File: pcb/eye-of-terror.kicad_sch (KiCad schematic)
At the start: 140 parts, among them J1 Conn_01x02_Socket, J2 G-Switch GT-USB-7055E, J3 Conn_01x04, J4 Conn_01x04, J5 Conn_01x03, J6 Conn_01x02_Socket, Q1 IPT020N10N3, Q2 IPT020N10N3, Q3 IPT020N10N3, Q4 IPT020N10N3, Q5 IPT020N10N3, Q6 IPT020N10N3, SW1 SW_Push, SW2 SW_Push, U1 RP2350B, U2 TD1660, U3 AP63205WU-7, U4 LSM6DS3, U5 W25Q32JVSS, U7 DRV8353HRTAR, Y1 ABM8-272-T3

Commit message: all footprints checked and added
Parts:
- C1, C39: footprint (none) -> Capacitor_SMD:CP_Elec_5x5.4
- J2: footprint (none) -> ul_GT-USB-7055A:CONN_GT-USB-7055A_GSW
- J3, J4: footprint (none) -> Connector_PinHeader_2.54mm:PinHeader_1x04_P2.54mm_Vertical
- J5: footprint (none) -> Connector_PinHeader_2.54mm:PinHeader_1x03_P2.54mm_Vertical
- JP1, JP10, JP11, JP12, JP13, JP14, JP15, JP2, JP3, JP4, JP5, JP6, JP7, JP8, JP9: footprint (none) -> Jumper:SolderJumper-2_P1.3mm_Bridged_RoundedPad1.0x1.5mm
- L1: footprint (none) -> inductor-muRataLQH5BPZ4R7NT0L:IND_LQH5BPZ4R7NT0L
- L2: footprint (none) -> Inductor_SMD:L_Sunlord_MWSA0402S
- SW1, SW2: footprint (none) -> Button_Switch_SMD:SW_Push_SPST_NO_Alps_SKRK
- U2: footprint (none) -> Techcode-Semicon-TD1660:TD1660-SOIC-8
- U3: footprint SOIC_05WU-7_DIO -> AP6320X-WU:SOIC_05WU-7_DIO
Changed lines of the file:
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@@
 			)
 		)
-		(property "Footprint" ""
+		(property "Footprint" "Jumper:SolderJumper-2_P1.3mm_Bridged_RoundedPad1.0x1.5mm"
 			(at 34.29 226.06 0)
 			(effects
@@
 			)
 		)
-		(property "Footprint" ""
+		(property "Footprint" "Connector_PinHeader_2.54mm:PinHeader_1x04_P2.54mm_Vertical"
 			(at 124.46 219.71 0)
 			(effects
@@
 			)
 		)
-		(property "Footprint" ""
+		(property "Footprint" "Jumper:SolderJumper-2_P1.3mm_Bridged_RoundedPad1.0x1.5mm"
 			(at 34.29 236.22 0)
 			(effects
@@
 			)
 		)
-		(property "Footprint" ""
+		(property "Footprint" "Jumper:SolderJumper-2_P1.3mm_Bridged_RoundedPad1.0x1.5mm"
 			(at 309.88 351.79 0)
 			(effects
@@
 			)
 		)
-		(property "Footprint" ""
+		(property "Footprint" "Jumper:SolderJumper-2_P1.3mm_Bridged_RoundedPad1.0x1.5mm"
 			(at 370.84 382.27 0)
 			(effects
@@
 			)
 		)
-		(property "Footprint" ""
+		(property "Footprint" "ul_GT-USB-7055A:CONN_GT-USB-7055A_GSW"
 			(at 107.95 386.08 0)
 			(effects
@@
 			)
 		)
-		(property "Footprint" ""
+		(property "Footprint" "Button_Switch_SMD:SW_Push_SPST_NO_Alps_SKRK"
 			(at 198.12 177.8 0)
 			(effects
@@
 			)
 		)
-		(property "Footprint" ""
+		(property "Footprint" "inductor-muRataLQH5BPZ4R7NT0L:IND_LQH5BPZ4R7NT0L"
 			(at 83.82 289.56 0)
 			(effects
@@
 			)
 		)
-		(property "Footprint" ""
+		(property "Footprint" "Button_Switch_SMD:SW_Push_SPST_NO_Alps_SKRK"
 			(at 212.09 156.21 0)
 			(effects
@@
 			)
 		)
-		(property "Footprint" ""
+		(property "Footprint" "Jumper:SolderJumper-2_P1.3mm_Bridged_RoundedPad1.0x1.5mm"
 			(at 34.29 241.3 0)
 			(effects
@@
 			)
 		)
-		(property "Footprint" ""
+		(property "Footprint" "Jumper:SolderJumper-2_P1.3mm_Bridged_RoundedPad1.0x1.5mm"
 			(at 34.29 238.76 0)
 			(effects
@@
 			)
 		)
-		(property "Footprint" ""
+		(property "Footprint" "Inductor_SMD:L_Sunlord_MWSA0402S"
 			(at 76.2 325.12 0)
 			(effects
@@
 			)
 		)
-		(property "Footprint" ""
+		(property "Footprint" "Connector_PinHeader_2.54mm:PinHeader_1x03_P2.54mm_Vertical"
 			(at 147.32 322.58 0)
 			(effects
@@
 			)
 		)
-		(property "Footprint" ""
+		(property "Footprint" "Jumper:SolderJumper-2_P1.3mm_Bridged_RoundedPad1.0x1.5mm"
 			(at 369.57 351.79 0)
 			(effects
@@
 			)
 		)
-		(property "Footprint" ""
+		(property "Footprint" "Jumper:SolderJumper-2_P1.3mm_Bridged_RoundedPad1.0x1.5mm"
 			(at 157.48 229.87 0)
 			(effects
@@
 			)
 		)
-		(property "Footprint" ""
+		(property "Footprint" "Jumper:SolderJumper-2_P1.3mm_Bridged_RoundedPad1.0x1.5mm"
 			(at 255.27 382.27 0)
 			(effects
@@
 			)
 		)
-		(property "Footprint" ""
+		(property "Footprint" "Jumper:SolderJumper-2_P1.3mm_Bridged_RoundedPad1.0x1.5mm"
 			(at 109.22 245.11 0)
 			(effects
@@
 			)
 		)
-		(property "Footprint" ""
+		(property "Footprint" "Capacitor_SMD:CP_Elec_5x5.4"
 			(at 256.54 208.28 0)
 			(effects
@@
 			)
 		)
-		(property "Footprint" ""
+		(property "Footprint" "Jumper:SolderJumper-2_P1.3mm_Bridged_RoundedPad1.0x1.5mm"
 			(at 311.15 382.27 0)
 			(effects
@@
 			)
 		)
-		(property "Footprint" ""
+		(property "Footprint" "Techcode-Semicon-TD1660:TD1660-SOIC-8"
 			(at 44.45 322.58 0)
 			(effects
@@
 			)
 		)
-		(property "Footprint" ""
+		(property "Footprint" "Jumper:SolderJumper-2_P1.3mm_Bridged_RoundedPad1.0x1.5mm"
 			(at 254 351.79 0)
 			(effects
@@
 			)
 		)
-		(property "Footprint" ""
+		(property "Footprint" "Connector_PinHeader_2.54mm:PinHeader_1x04_P2.54mm_Vertical"
 			(at 124.46 242.57 0)
 			(effects
@@
 			)
 		)
-		(property "Footprint" ""
+		(property "Footprint" "Jumper:SolderJumper-2_P1.3mm_Bridged_RoundedPad1.0x1.5mm"
 			(at 109.22 247.65 0)
 			(effects
@@
 			)
 		)
-		(property "Footprint" ""
+		(property "Footprint" "Capacitor_SMD:CP_Elec_5x5.4"
 			(at 22.86 293.37 0)
 			(effects
@@
 			)
 		)
-		(property "Footprint" ""
+		(property "Footprint" "Jumper:SolderJumper-2_P1.3mm_Bridged_RoundedPad1.0x1.5mm"
 			(at 109.22 224.79 0)
 			(effects
@@
 			)
 		)
-		(property "Footprint" ""
+		(property "Footprint" "Jumper:SolderJumper-2_P1.3mm_Bridged_RoundedPad1.0x1.5mm"
 			(at 109.22 222.25 0)
 			(effects
@@
 			)
 		)
-		(property "Footprint" "SOIC_05WU-7_DIO"
+		(property "Footprint" "AP6320X-WU:SOIC_05WU-7_DIO"
 			(at 44.45 287.02 0)
 			(effects

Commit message: added extra breakout GPIO pins, imported PCB DXF
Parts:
- added J10, J11, J12, J13, J14, J15, J16, J8, J9: Conn_01x03, Connector_PinHeader_2.54mm:PinHeader_1x03_P2.54mm_Vertical, symbol Connector_Generic:Conn_01x03
- added J7: Conn_01x02_Socket, Connector_AMASS:AMASS_XT60-M_1x02_P7.20mm_Vertical, symbol Connector:Conn_01x02_Socket
- added JP16: SolderJumper_2_Bridged, Jumper:SolderJumper-2_P1.3mm_Bridged_RoundedPad1.0x1.5mm, symbol Jumper:SolderJumper_2_Bridged
- added JP17, JP18, JP19, JP20, JP21, JP22, JP23, JP24, JP25: SolderJumper_3_Open, Jumper:SolderJumper-3_P1.3mm_Open_RoundedPad1.0x1.5mm, symbol Jumper:SolderJumper_3_Open
- J3, J4: footprint Connector_PinHeader_2.54mm:PinHeader_1x04_P2.54mm_Vertical -> Connector_PinHeader_1.00mm:PinHeader_1x04_P1.00mm_Vertical
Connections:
- net +3V3: now also JP17.3 (B), JP18.3 (B), JP19.3 (B), JP20.3 (B), JP21.3 (B), JP22.3 (B), JP23.3 (B), JP24.3 (B), JP25.3 (B)
- net +5V: now also JP17.1 (A), JP18.1 (A), JP19.1 (A), JP20.1 (A), JP21.1 (A), JP22.1 (A), JP23.1 (A), JP24.1 (A), JP25.1 (A)
- net +BATT: now also JP16.2 (B); no longer D18.2 (A)
- net +BATT_RAW: now also J7.1 (Pin_1)
- net AGND: now also J10.3 (Pin_3), J11.3 (Pin_3), J12.3 (Pin_3), J13.3 (Pin_3), J14.3 (Pin_3), J15.3 (Pin_3), J16.3 (Pin_3), J7.2 (Pin_2), J8.3 (Pin_3), J9.3 (Pin_3)
- net GPIO24: now reaches U1.25 (GPIO24)
- net GPIO24: now also J11.1 (Pin_1)
- net GPIO34: now reaches U1.43 (GPIO34)
- net GPIO34: now also J12.1 (Pin_1)
- net GPIO35: now reaches U1.44 (GPIO35)
- net GPIO35: now also J13.1 (Pin_1)
- net GPIO37: now reaches U1.46 (GPIO37)
- net GPIO37: now also J14.1 (Pin_1)
- net GPIO38: now reaches U1.47 (GPIO38)
- net GPIO38: now also J15.1 (Pin_1)
- net GPIO39: now reaches U1.48 (GPIO39)
- net GPIO39: now also J16.1 (Pin_1)
- net GPIO1: now reaches U1.78 (GPIO1)
- net GPIO1: now also J8.1 (Pin_1)
- net GPIO2: now reaches U1.79 (GPIO2)
- net GPIO2: now also J9.1 (Pin_1)
- net GPIO3: now reaches U1.80 (GPIO3)
- net GPIO3: now also J10.1 (Pin_1)
- new net: J8.2 (Pin_2), JP17.2 (C)
- new net: D18.2 (A), JP16.1 (A)
- new net: J10.2 (Pin_2), JP19.2 (C)
- new net: J16.2 (Pin_2), JP25.2 (C)
- new net: J11.2 (Pin_2), JP20.2 (C)
- new net: J15.2 (Pin_2), JP24.2 (C)
- new net: J9.2 (Pin_2), JP18.2 (C)
- new net: J14.2 (Pin_2), JP23.2 (C)
- new net: J13.2 (Pin_2), JP22.2 (C)
- new net: J12.2 (Pin_2), JP21.2 (C)
- no-connect marks 13 -> 4
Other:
- note added: "Battery Plugs"
- note added: "Cut this jumper if the LED always being on gets too annoying."
- note added: "Extra GPIO Breakout Pins"
- note added: "This pinout follows Adafruit's STEMMA QT cables. The connectors they use are JST-SH 4-pin, 1mm pitch."
- note removed: "Battery Plug"
- note removed: "This pinout follows Adafruit's STEMMA QT cables."
- moved on the sheet: D18, J1, R40

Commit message: WIP layout, most components placed
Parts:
- added H1, H10, H11, H12, H13, H14, H15, H16, H17, H18, H19, H2, H20, H21, H22, H23, H24, H25, H26, H27, H28, H29, H3, H30, H31, H32, H33, H34, H35, H36, H37, H38, H39, H4, H40, H41, H42, H43, H44, H45, H46, H47, H48, H49, H5, H50, H51, H52, H53, H54, H6, H7, H8, H9: MountingHole, MountingHole:MountingHole_3.2mm_M3, symbol Mechanical:MountingHole
- added NT1: NetTie_3, NetTie:NetTie-3_SMD_Pad2.0mm, symbol Device:NetTie_3
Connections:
- net +BATT_RAW: now also J1.2 (Pin_2), J7.2 (Pin_2); no longer J1.1 (Pin_1), J7.1 (Pin_1)
- net AGND: now also NT1.2; no longer C1.2, C10.1, C11.1, C12.1, C13.1, C14.1, C15.1, C16.1, C17.1, C18.1, C19.1, C20.1, C21.1, C22.1, C23.1, C24.1, C25.1, C26.1, C27.1, C28.1, C29.1, C3.2, C30.1, C33.1, C34.1, C36.1, C37.1, C38.1, C39.1, C4.2, C6.2, C7.2, C8.2, D1.2 (A2), D2.2 (A), J1.2 (Pin_2), J10.3 (Pin_3), J11.3 (Pin_3), J12.3 (Pin_3), J13.3 (Pin_3), J14.3 (Pin_3), J15.3 (Pin_3), J16.3 (Pin_3), J2.A1/B12 (GND), J2.B1/A12 (GND), J3.1 (Pin_1), J4.1 (Pin_1), J5.2 (Pin_2), J7.2 (Pin_2), J8.3 (Pin_3), J9.3 (Pin_3), R1.1, R10.2, R17.2, R18.2, R19.2, R2.1, R21.2, R23.2, R24.2, R25.2, R26.2, R27.2, R28.2, R29.2, R30.2, R31.2, R32.2, R33.2, R34.2, R35.2, R36.2, R37.2, R38.2, R39.2, R4.2, R40.1, R5.2, R6.2, SW1.2, U1.62 (VREG_PGND), U1.81 (GND), U2.5 (GND), U3.4 (GND), U4.2 (SDX), U4.3 (SCX), U4.4 (INT1), U4.6 (GND), U4.7 (GND), U4.9 (INT2), U5.4 (GND), U6.4 (GND), U7.10 (SNA), U7.11 (SNB), U7.20 (SNC), U7.39 (GND), U7.41 (PAD)
- net GND renamed DGND
- net DGND: now also C10.1, C11.1, C12.1, C13.1, C14.1, C15.1, C16.1, C17.1, C18.1, C19.1, C20.1, C21.1, C22.1, C23.1, C24.1, C25.1, C26.1, C27.1, C28.1, C29.1, C33.1, C34.1, J10.3 (Pin_3), J11.3 (Pin_3), J12.3 (Pin_3), J13.3 (Pin_3), J14.3 (Pin_3), J15.3 (Pin_3), J16.3 (Pin_3), J2.A1/B12 (GND), J2.B1/A12 (GND), J3.1 (Pin_1), J4.1 (Pin_1), J5.2 (Pin_2), J8.3 (Pin_3), J9.3 (Pin_3), R1.1, R10.2, R2.1, R25.2, R26.2, R27.2, R28.2, R29.2, R30.2, R31.2, R32.2, R33.2, R34.2, R35.2, R36.2, R37.2, R38.2, R39.2, R40.1, SW1.2, U1.62 (VREG_PGND), U1.81 (GND), U4.2 (SDX), U4.3 (SCX), U4.4 (INT1), U4.6 (GND), U4.7 (GND), U4.9 (INT2), U5.4 (GND), U6.4 (GND), U7.39 (GND), NT1.3
- new net PGND: C1.2, C3.2, C30.1, C36.1, C37.1, C38.1, C39.1, C4.2, C6.2, C7.2, C8.2, D1.2 (A2), D2.2 (A), J1.1 (Pin_1), J7.1 (Pin_1), NT1.1, R17.2, R18.2, R19.2, R21.2, R23.2, R24.2, R4.2, R5.2, R6.2, U2.5 (GND), U3.4 (GND), U7.10 (SNA), U7.11 (SNB), U7.20 (SNC), U7.41 (PAD)
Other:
- note added: "Mounting Holes"

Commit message: WIP layout
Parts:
- removed JP8: SolderJumper_2_Bridged, Jumper:SolderJumper-2_P1.3mm_Bridged_RoundedPad1.0x1.5mm, symbol Jumper:SolderJumper_2_Bridged
- removed R24: 10k, Resistor_SMD:R_0402_1005Metric, symbol Device:R_Small_US
- added NT2, NT3, NT4, NT5, NT6: NetTie_2, NetTie:NetTie-2_SMD_Pad2.0mm, symbol Device:NetTie_2
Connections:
- net +3V3: no longer U1.53 (GPIO42_ADC2)
- net 5V_MON: now also U1.58 (GPIO47_ADC7); no longer U1.52 (GPIO41_ADC1)
- net BATT_MON: now also U1.57 (GPIO46_ADC6); no longer U1.49 (GPIO40_ADC0)
- net DGND: now also NT2.2, NT3.2, NT4.2, NT5.2, NT6.2
- net GPIO0: now also R9.2, U5.1 (~{CS})
- net PGND: now also NT2.1, NT3.1, NT4.1, NT5.1, NT6.1
- net SOA: now also U1.54 (GPIO43_ADC3); no longer U1.56 (GPIO45_ADC5)
- net SOC: now also U1.56 (GPIO45_ADC5); no longer U1.54 (GPIO43_ADC3)
- no-connect marks 4 -> 5
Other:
- note added: "Isolating power ground, digital ground, and analog ground."
- note removed: "Future-proofing schematic in case it turns out that power ground, digital ground, and analog ground need to be separated and connect together at one point only."
- moved on the sheet: NT1, U6

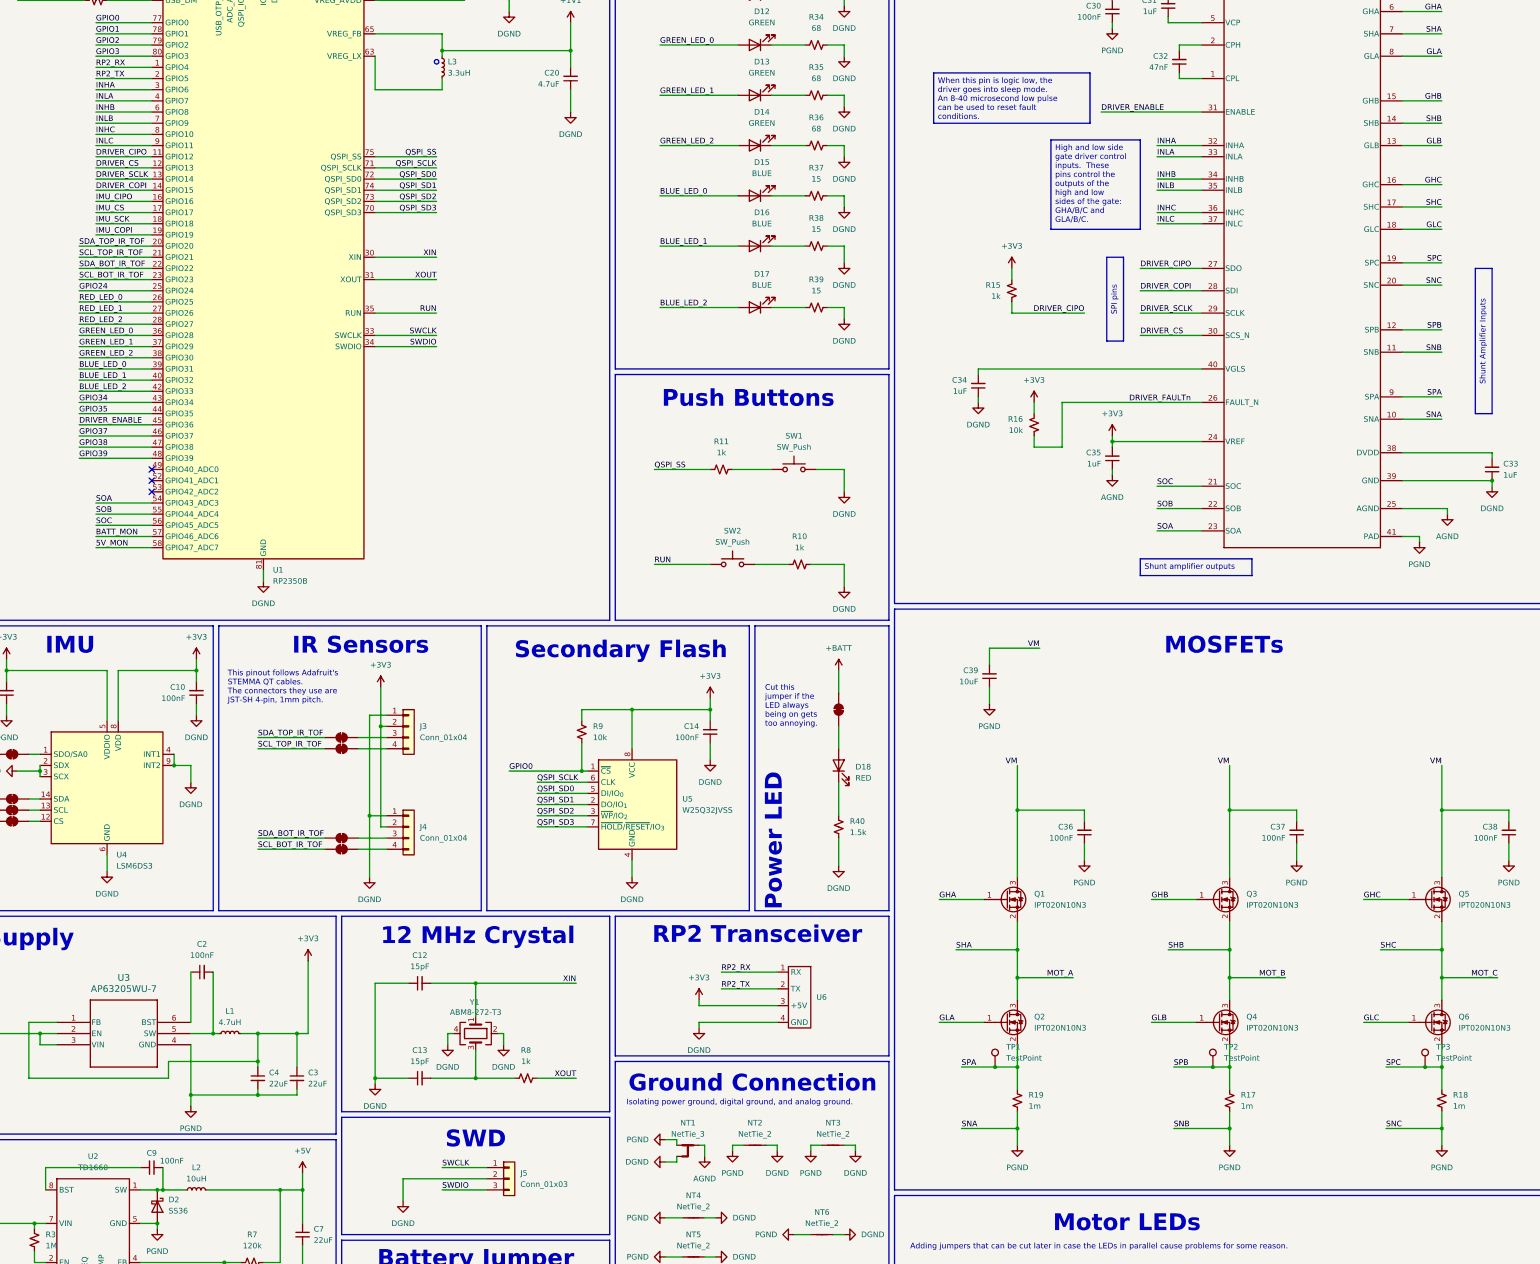
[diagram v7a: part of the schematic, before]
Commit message: re-routed mosfets for better layout
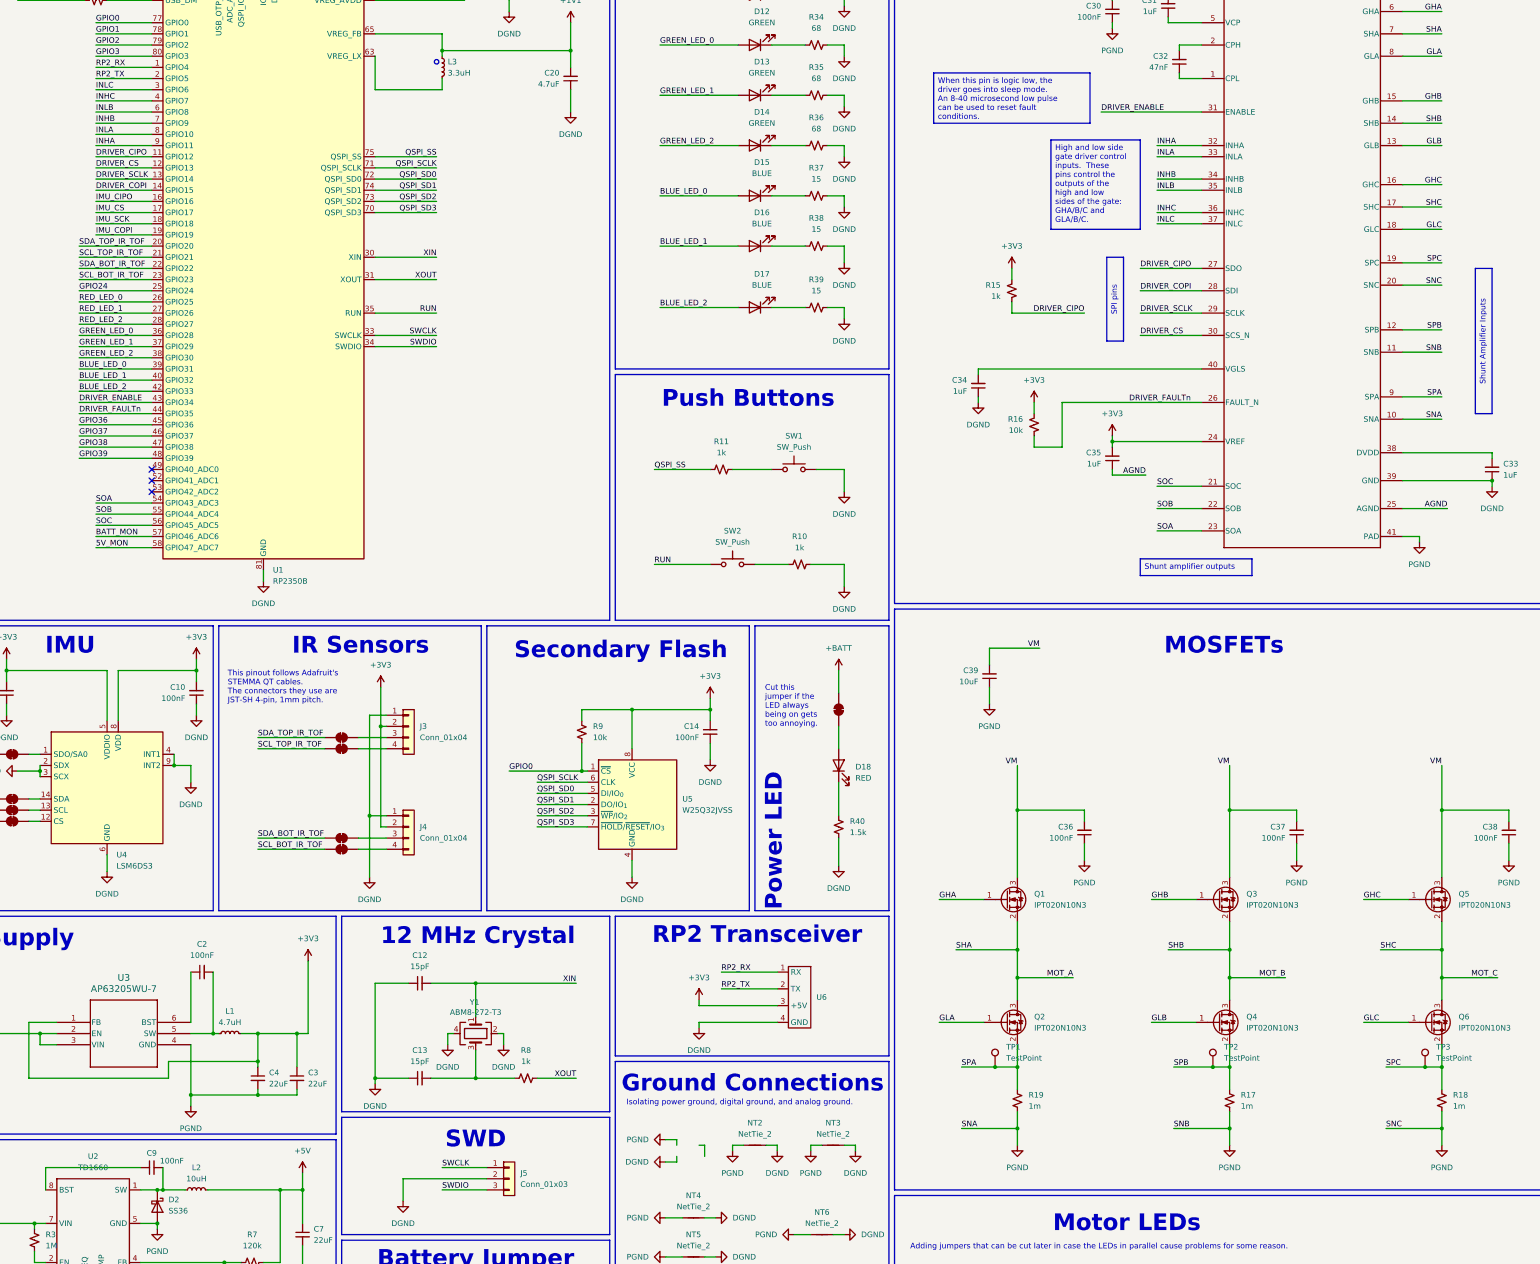
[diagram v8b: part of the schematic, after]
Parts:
- removed NT1: NetTie_3, NetTie:NetTie-3_SMD_Pad2.0mm, symbol Device:NetTie_3
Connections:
- net DRIVER_ENABLE: now also U1.43 (GPIO34); no longer U1.45 (GPIO36)
- net DRIVER_FAULTn: now also U1.44 (GPIO35)
- net GPIO34: no longer U1.43 (GPIO34)
- net GPIO35: no longer U1.44 (GPIO35)
- net INHA: now also U1.9 (GPIO11); no longer U1.3 (GPIO6)
- net INHB: now also U1.7 (GPIO9); no longer U1.6 (GPIO8)
- net INHC: now also U1.4 (GPIO7); no longer U1.8 (GPIO10)
- net INLA: now also U1.8 (GPIO10); no longer U1.4 (GPIO7)
- net INLB: now also U1.6 (GPIO8); no longer U1.7 (GPIO9)
- net INLC: now also U1.3 (GPIO6); no longer U1.9 (GPIO11)
- new net GPIO36: U1.45 (GPIO36)
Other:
- note added: "Ground Connections"
- note removed: "Ground Connection"
